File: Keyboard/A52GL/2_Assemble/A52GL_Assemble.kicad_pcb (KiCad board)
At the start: 2 copper layers, 305.8 x 99.2 mm, 109 parts, among them J1 Conn_01x02, SW1 SW_PUSH, SW10 SW_PUSH, SW11 SW_PUSH, SW12 SW_PUSH, SW13 SW_PUSH, SW14 SW_PUSH, SW15 SW_PUSH, SW16 SW_PUSH, SW17 SW_PUSH, SW18 SW_PUSH, SW19 SW_PUSH, SW2 SW_PUSH, SW20 SW_PUSH, SW21 SW_PUSH, SW22 SW_PUSH, SW23 SW_PUSH, SW24 SW_PUSH, SW25 SW_PUSH, SW26 SW_PUSH, SW27 SW_PUSH, SW28 SW_PUSH, SW29 SW_PUSH, SW3 SW_PUSH, SW30 SW_PUSH, SW31 SW_PUSH, SW32 SW_PUSH, SW33 SW_PUSH, SW34 SW_PUSH, SW35 SW_PUSH, SW36 SW_PUSH, SW37 SW_PUSH, SW38 SW_PUSH, SW39 SW_PUSH, SW4 SW_PUSH, SW40 SW_PUSH, SW41 SW_PUSH, SW42 SW_PUSH, SW43 SW_PUSH, SW44 SW_PUSH, SW45 SW_PUSH, SW46 SW_PUSH, SW47 SW_PUSH, SW48 SW_PUSH, SW49 SW_PUSH, SW5 SW_PUSH, SW50 SW_PUSH, SW51 SW_PUSH, SW52 SW_PUSH, SW53 SW_PUSH, SW6 SW_PUSH, SW7 SW_PUSH, SW8 SW_PUSH, SW9 SW_PUSH, U1 BLEMicroPro

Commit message: 寸法更新とか
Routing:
- net Col0: track 543.5 -> 539.5 mm
- net Col6: track 355.4 -> 357.5 mm
- net Col1: track 565.6 -> 567.7 mm
- net Col4: track 407.2 -> 405.8 mm
- net Col5: track 383.9 -> 382.6 mm
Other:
- board size 305.8 x 99.2 mm -> 304.4 x 98.8 mm

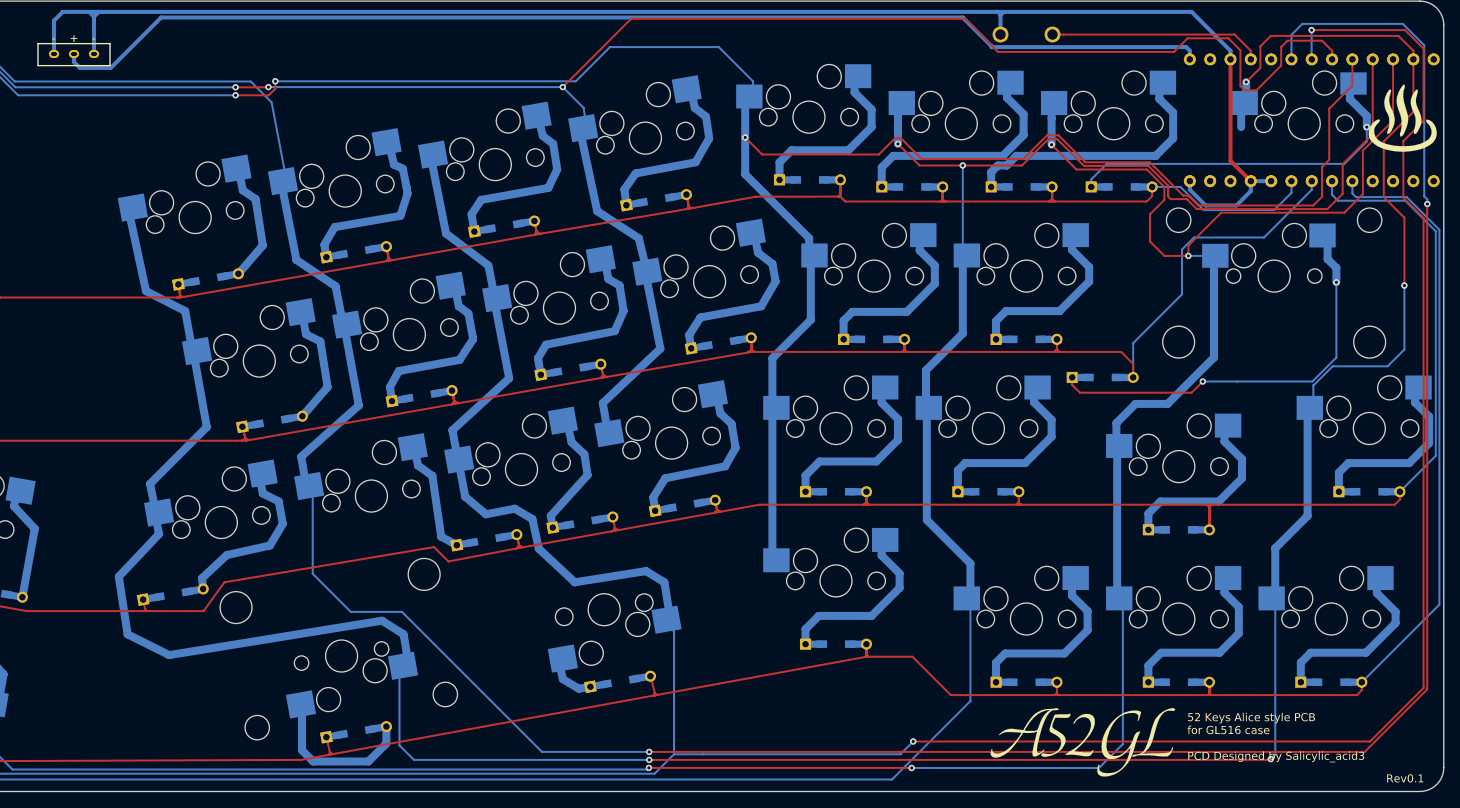
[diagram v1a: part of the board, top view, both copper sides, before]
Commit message: 電池コネクタの更新、シルクの修正
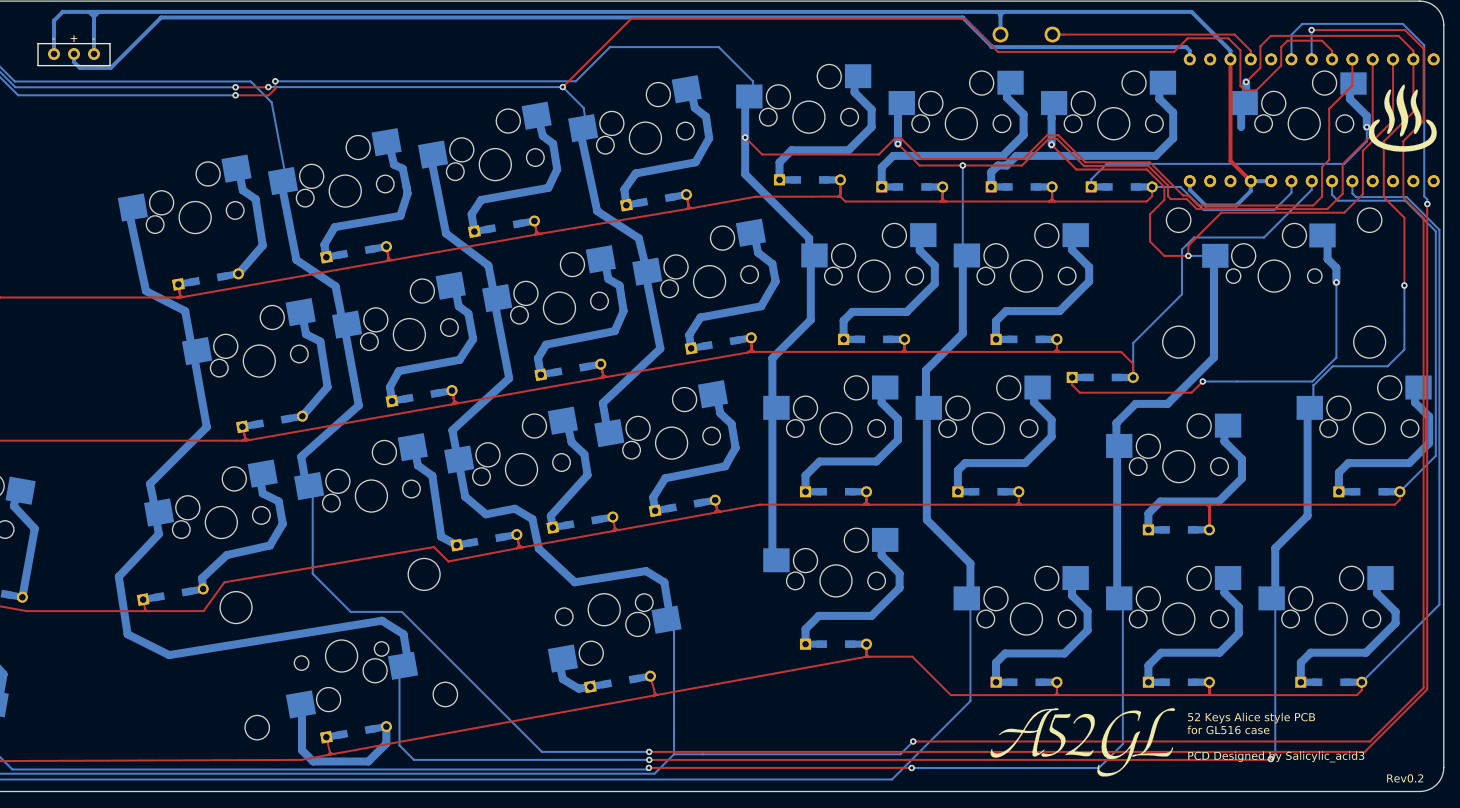
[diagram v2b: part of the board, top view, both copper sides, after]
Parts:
- J1: footprint kbd_Parts:Battery_XH2.5_GL_rev -> kbd_Parts:Battery_XH2.5_GL_PCB
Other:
- board text added: "Rev0.2"
- board text removed: "Rev0.1"
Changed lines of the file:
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@@
   )
   (setup
-    (last_trace_width 1)
+    (last_trace_width 0.25)
     (user_trace_width 0.5)
     (user_trace_width 0.9)
@@
     (add_net VCC)
   )
+  (module kbd_Parts:Battery_XH2.5_GL_PCB (layer B.Cu)
+    (at 152.4 23.8125 180)
+    (fp_text reference J1 (at -3 2) (layer B.Fab)
+      (effects (font (size 1 1) (thickness 0.15)) (justify mirror))
+    )
+    (fp_text value Conn_01x02 (at 0 -3.5) (layer B.Fab) hide
+      (effects (font (size 1 1) (thickness 0.15)) (justify mirror))
+    )
+    (fp_line (start 4.5 1.25) (end 4.5 -1.5) (layer F.SilkS) (width 0.15))
+    (fp_line (start 4.5 -1.5) (end -4.5 -1.5) (layer F.SilkS) (width 0.15))
+    (fp_line (start -4.5 1.25) (end 4.5 1.25) (layer F.SilkS) (width 0.15))
+    (fp_line (start -4.5 -1.5) (end -4.5 1.25) (layer F.SilkS) (width 0.15))
+    (fp_line (start 4.5 1.25) (end 4.5 -1.5) (layer B.SilkS) (width 0.15))
+    (fp_line (start -4.5 1.25) (end 4.5 1.25) (layer B.SilkS) (width 0.15))
+    (fp_line (start -4.5 -1.5) (end -4.5 1.25) (layer B.SilkS) (width 0.15))
+    (fp_line (start 4.5 -1.5) (end -4.5 -1.5) (layer B.SilkS) (width 0.15))
+    (fp_text user XH2.5 (at 1.25 2) (layer B.SilkS) hide
+      (effects (font (size 1 1) (thickness 0.15)) (justify mirror))
+    )
+    (pad 2 thru_hole oval (at -2.5 -0.05 180) (size 1.5 1.5) (drill oval 0.8) (layers *.Cu *.Mask)
+      (net 57 GND) (clearance 0.15))
+    (pad 1 thru_hole oval (at 0 -0.05 180) (size 1.5 1.5) (drill oval 0.8) (layers *.Cu *.Mask)
+      (net 58 Bat+) (clearance 0.15))
+    (pad 2 thru_hole oval (at 2.5 -0.05 180) (size 1.5 1.5) (drill oval 0.8) (layers *.Cu *.Mask)
+      (net 57 GND) (clearance 0.15))
+    (model "../../../../../../Users/pluis/Documents/Magic Briefcase/Documents/KiCad/3d/AB2_TRS_3p5MM_PTH.wrl"
+      (at (xyz 0 0 0))
+      (scale (xyz 0.42 0.42 0.42))
+      (rotate (xyz 0 0 90))
+    )
+  )
   (module logos:onsen (layer F.Cu)
     (at 318.47 31.86)
@@
       (xy 5.989872 -3.961898) (xy 6.274975 -3.981652) (xy 6.532227 -3.976181)) (layer F.SilkS) (width 0.01))
   )
-  (module kbd_Parts:Battery_XH2.5_GL_rev (layer B.Cu)
-    (at 152.4 23.8125 180)
-    (fp_text reference J1 (at -3 2) (layer B.Fab)
-      (effects (font (size 1 1) (thickness 0.15)) (justify mirror))
-    )
-    (fp_text value Conn_01x02 (at 0 -3.5) (layer B.Fab) hide
-      (effects (font (size 1 1) (thickness 0.15)) (justify mirror))
-    )
-    (fp_line (start -4.5 -1.5) (end -4.5 1.25) (layer F.SilkS) (width 0.15))
-    (fp_line (start -4.5 1.25) (end 4.5 1.25) (layer F.SilkS) (width 0.15))
-    (fp_line (start 4.5 -1.5) (end -4.5 -1.5) (layer F.SilkS) (width 0.15))
-    (fp_line (start 4.5 1.25) (end 4.5 -1.5) (layer F.SilkS) (width 0.15))
-    (fp_line (start 4.5 1.25) (end 4.5 -1.5) (layer B.SilkS) (width 0.15))
-    (fp_line (start -4.5 1.25) (end 4.5 1.25) (layer B.SilkS) (width 0.15))
-    (fp_line (start -4.5 -1.5) (end -4.5 1.25) (layer B.SilkS) (width 0.15))
-    (fp_line (start 4.5 -1.5) (end -4.5 -1.5) (layer B.SilkS) (width 0.15))
-    (fp_text user XH2.5 (at 1.25 2) (layer B.SilkS) hide
-      (effects (font (size 1 1) (thickness 0.15)) (justify mirror))
-    )
-    (pad 2 thru_hole oval (at -2.5 -0.05 180) (size 1.3 1) (drill oval 0.8 0.5) (layers *.Cu *.Mask)
-      (net 57 GND) (clearance 0.15))
-    (pad 1 thru_hole oval (at 0 -0.05 180) (size 1.3 1) (drill oval 0.8 0.5) (layers *.Cu *.Mask)
-      (net 58 Bat+) (clearance 0.15))
-    (pad 2 thru_hole oval (at 2.5 -0.05 180) (size 1.3 1) (drill oval 0.8 0.5) (layers *.Cu *.Mask)
-      (net 57 GND) (clearance 0.15))
-    (model "../../../../../../Users/pluis/Documents/Magic Briefcase/Documents/KiCad/3d/AB2_TRS_3p5MM_PTH.wrl"
-      (at (xyz 0 0 0))
-      (scale (xyz 0.42 0.42 0.42))
-      (rotate (xyz 0 0 90))
-    )
-  )
   (module kbd_Parts:ResetSW (layer F.Cu)
     (at 271.4625 21.43125)
@@
       (net 54 "Net-(D50-Pad1)"))
   )
-  (gr_text Rev0.1 (at 318.8 114.45) (layer F.SilkS)
+  (gr_text Rev0.2 (at 318.8 114.45) (layer F.SilkS)
     (effects (font (size 1 1) (thickness 0.1)))
   )

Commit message: シンボル、フットプリントの更新に合わせて更新
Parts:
- SW50: footprint kbd:CherryMX_Hotswap_BL_LH_v2_ -> kbd_SW:CherryMX_Hotswap_1.0u_Small1

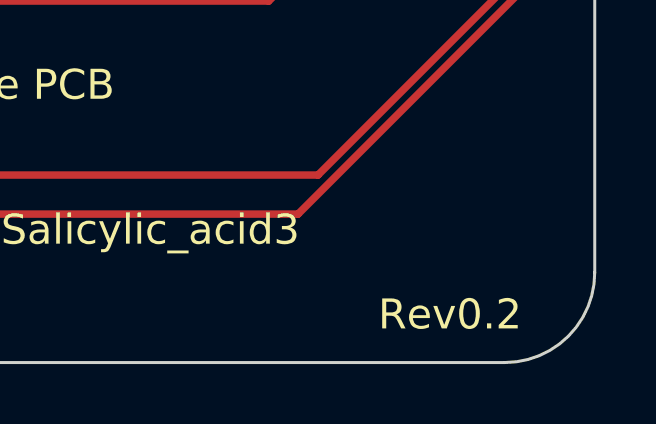
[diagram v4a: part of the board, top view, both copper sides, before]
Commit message: フットプリント名の変更に対応
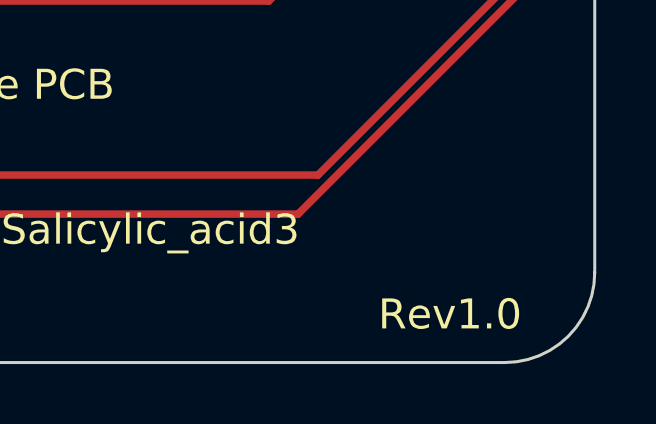
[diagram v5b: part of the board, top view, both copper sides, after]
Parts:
- SW1, SW10, SW11, SW12, SW13, SW14, SW15, SW16, SW17, SW18, SW20, SW21, SW22, SW23, SW24, SW25, SW26, SW28, SW29, SW30, SW31, SW32, SW33, SW35, SW36, SW37, SW38, SW39, SW40, SW41, SW42, SW43, SW44, SW45, SW46, SW48, SW49, SW5, SW51, SW52, SW6, SW7, SW9: footprint kbd_SW:CherryMX_Hotswap_1.0u -> kbd_SW:CherryMX_Hotswap_1u
- SW50: footprint kbd_SW:CherryMX_Hotswap_1.0u_Small1 -> kbd_SW:CherryMX_Hotswap_1u_Small1
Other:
- board text added: "Rev1.0"
- board text removed: "Rev0.2"

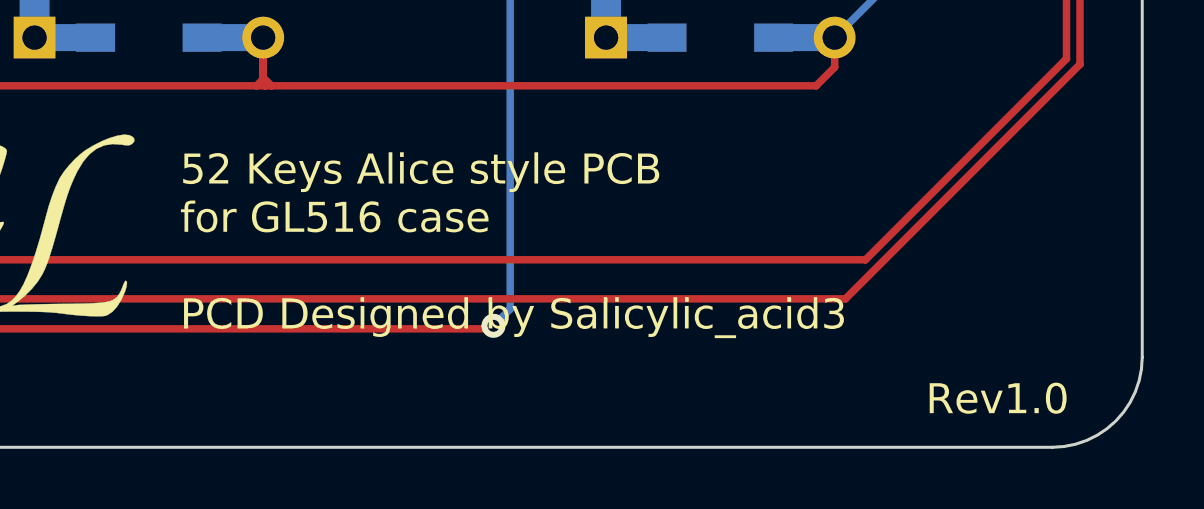
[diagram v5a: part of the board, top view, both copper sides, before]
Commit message: 電池プレートの修正
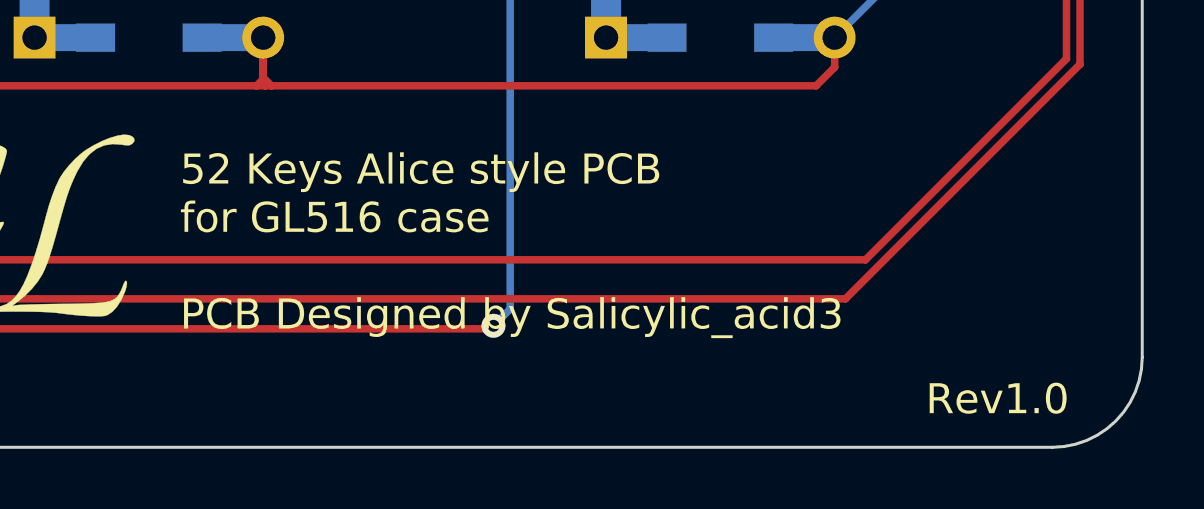
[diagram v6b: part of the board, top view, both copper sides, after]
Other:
- board text added: "52 Keys Alice style PCB for GL516 case PCB Designed by Salicylic_acid3"
- board text removed: "52 Keys Alice style PCB for GL516 case PCD Designed by Salicylic_acid3"
